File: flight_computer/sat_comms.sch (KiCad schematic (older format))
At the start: 1 part

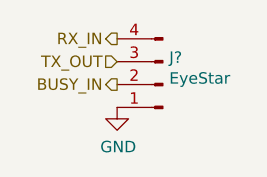
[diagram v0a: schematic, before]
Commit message: Annotating schematic with references and footprints
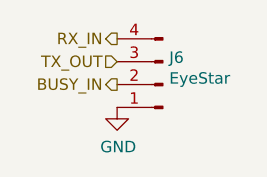
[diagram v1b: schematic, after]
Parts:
- gave numbers to parts that had none: 1
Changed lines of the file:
@@
 $EndDescr
 $Comp
-L Connector:Conn_01x04_Male J?
+L Connector:Conn_01x04_Male J6
 U 1 1 637A3118
 P 6050 3600
-F 0 "J?" H 6022 3482 50  0000 R CNN
+F 0 "J6" H 6022 3482 50  0000 R CNN
 F 1 "EyeStar" H 6022 3573 50  0000 R CNN
 F 2 "" H 6050 3600 50  0001 C CNN
@@
 $EndComp
 $Comp
-L power:GND #PWR?
+L power:GND #PWR0289
 U 1 1 637A3C71
 P 5850 3700
-F 0 "#PWR?" H 5850 3450 50  0001 C CNN
+F 0 "#PWR0289" H 5850 3450 50  0001 C CNN
 F 1 "GND" H 5855 3527 50  0000 C CNN
 F 2 "" H 5850 3700 50  0001 C CNN
